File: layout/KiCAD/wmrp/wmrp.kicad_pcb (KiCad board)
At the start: 2 copper layers, 2 parts, among them U1 AD8552

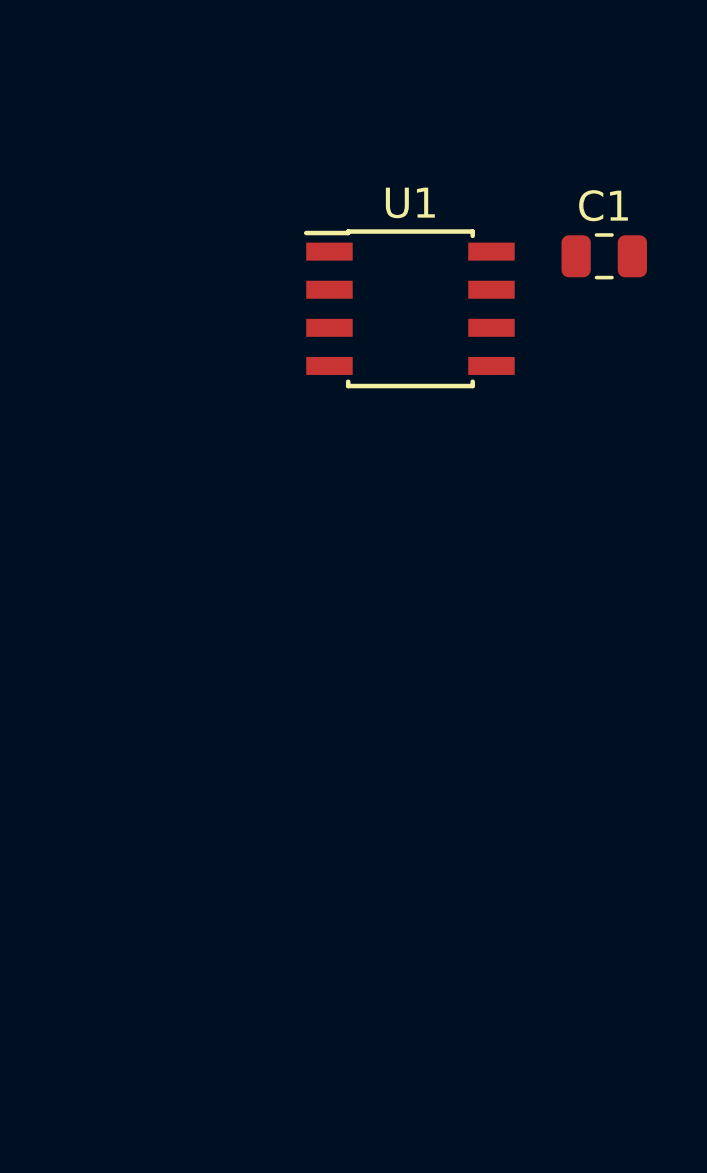
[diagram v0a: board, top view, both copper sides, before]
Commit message: First try to use instrumentation amplifier for thermocouple reading
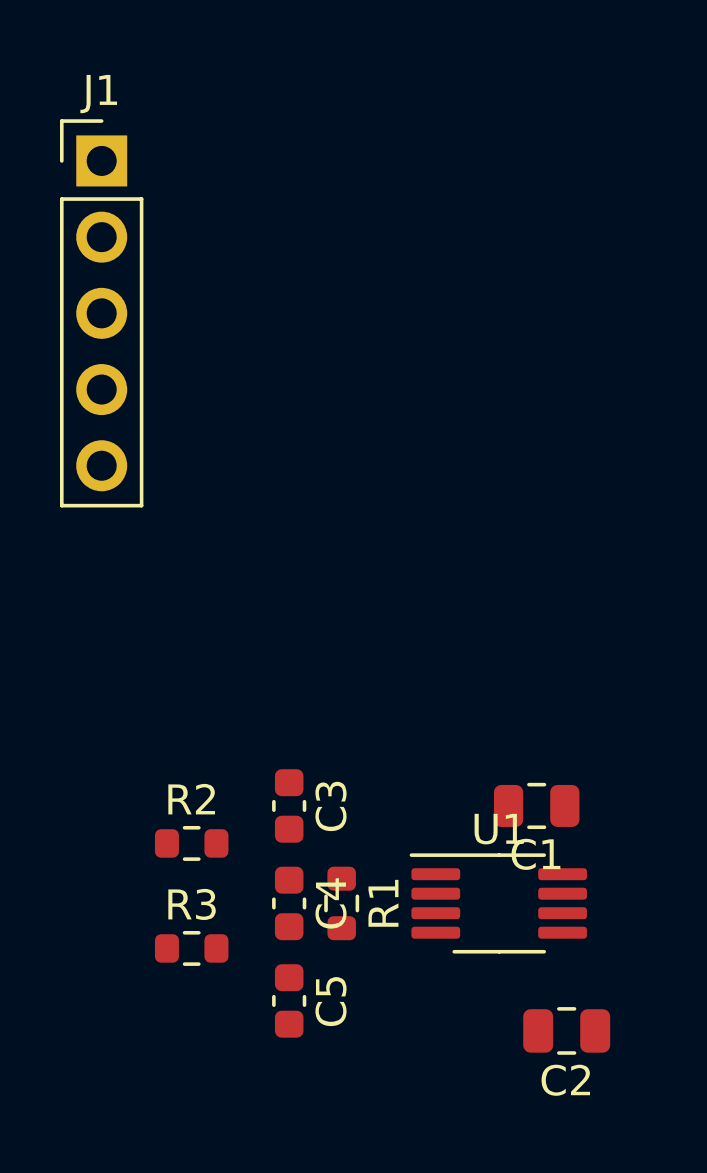
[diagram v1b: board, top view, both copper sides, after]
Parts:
- added C2: 100nF, Capacitor_SMD:C_0805_2012Metric, F.Cu at (110.0, 148.2)
- added C3: 1nF, Capacitor_SMD:C_0603_1608Metric, F.Cu at (100.8, 140.8)
- added C4: 22nF, Capacitor_SMD:C_0603_1608Metric, F.Cu at (100.8, 144.0)
- added C5: 1nF, Capacitor_SMD:C_0603_1608Metric, F.Cu at (100.8, 147.2)
- added J1: DIN-5, Connector_PinHeader_2.54mm:PinHeader_1x05_P2.54mm_Vertical, F.Cu at (94.5, 119.2)
- added R1: 1k, Resistor_SMD:R_0603_1608Metric, F.Cu at (102.5, 144.0)
- added R2: 22k, Resistor_SMD:R_0603_1608Metric, F.Cu at (97.5, 142.0)
- added R3: 22k, Resistor_SMD:R_0603_1608Metric, F.Cu at (97.5, 145.5)
- U1: value AD8552 -> AD8236; footprint Package_SO:SOIC-8_3.9x4.9mm_P1.27mm -> Package_SO:MSOP-8_3x3mm_P0.65mm
- moved U1 20.0 mm to (107.8, 144.0)
- moved C1 18.5 mm to (109.0, 140.8), turned to 180 degrees
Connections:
- U1 pad 4: GND -> Net-(U1-Pad4)
- U1 pad 5: (no net) -> -5V
- U1 pad 6: (no net) -> GND
- U1 pad 7: (no net) -> /TIP_TEMP
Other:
- net class Default removed
